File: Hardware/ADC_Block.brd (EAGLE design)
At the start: 30.5 x 44.5 mm, 34 parts, among them U1 ADS1015, U2 PCA9306, U3 3.3V

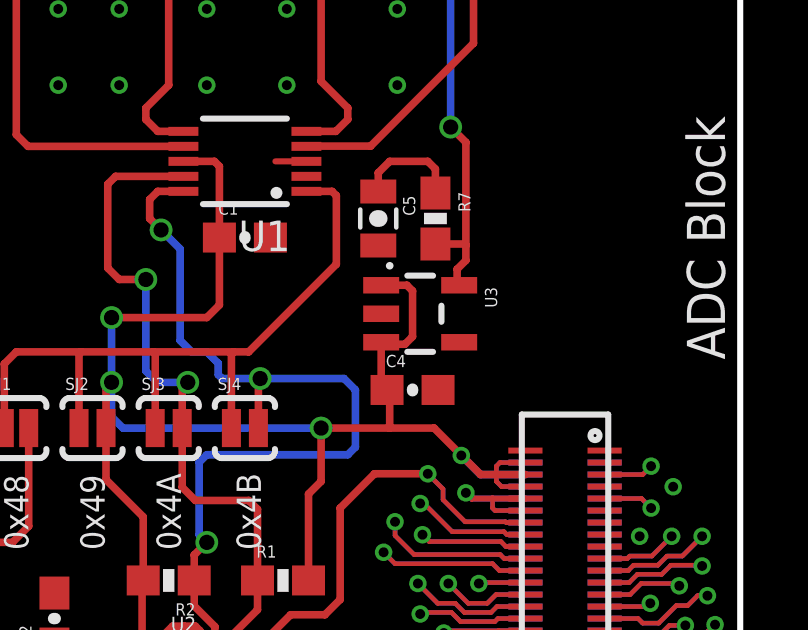
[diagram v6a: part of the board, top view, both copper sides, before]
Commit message: Moved pin 1 markers to outside packages on IC and Hirose connectors.
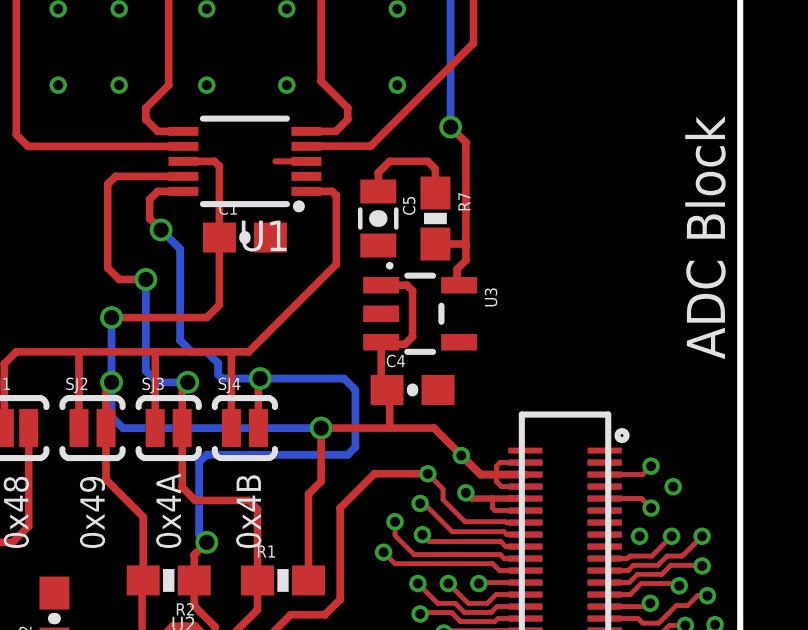
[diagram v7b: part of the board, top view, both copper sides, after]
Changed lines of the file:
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@@
 <layer number="45" name="Holes" color="7" fill="1" visible="yes" active="yes"/>
 <layer number="46" name="Milling" color="3" fill="1" visible="no" active="yes"/>
-<layer number="47" name="Measures" color="7" fill="1" visible="no" active="yes"/>
+<layer number="47" name="Measures" color="7" fill="1" visible="yes" active="yes"/>
 <layer number="51" name="tDocu" color="6" fill="1" visible="yes" active="yes"/>
 <layer number="52" name="bDocu" color="7" fill="1" visible="no" active="yes"/>
@@
 </class>
 </classes>
-<designrules name="Gold_Phoenix_Standard_Spec_2_layer">
-<description language="en">&lt;b&gt;EAGLE Design Rules&lt;/b&gt;
+<designrules name="SparkFun-2-layer-FAB-LIMIT">
+<description language="en">&lt;b&gt;SparkFun 2 Layer Design Rule Checks - STANDARD/TIGHT/FAB-LIMIT&lt;/b&gt;
 &lt;p&gt;
-The default Design Rules have been set to cover
-a wide range of applications. Your particular design
-may have different requirements, so please make the
-necessary adjustments and save your customized
-design rules under a new name.</description>
+These rules have been curated by SparkFuns DFM commitee. After doing much research, communicating with our multiple fab houses, and getting quotes of various designs, we have compiled three DRU files.
+&lt;p&gt;
+&lt;b&gt;STANDARD:&lt;/b&gt; This is more of a &quot;best case scenario&quot; set of limitations. If your design has the space, and/or you have the time to work within these parameters, please do. Larger trace width and clearance makes for easier visual inspection of the PCB while troubleshooting (useful in production and to the end user). It also allows for better ability to hack a trace (if you are crazy enough to scrape away the mask and solder to a trace). Another thing to keep in mind is that more metal is just more robust.
+&lt;p&gt;
+&lt;b&gt;TIGHT:&lt;/b&gt; This is where cost comes into play. We have found that most fab houses begin to add extra charges when you go smaller than these specs. In some cases, going to less than 15 mil trace can increase the cost by 10%. (This is why we have set the min drill on this DRU to 15 mil) Same story for traces thinner than 7 mil. To avoid those extra charges, then stay within the rules of this DRU.
+&lt;p&gt;
+&lt;b&gt;FAB-LIMIT:&lt;/b&gt; These set of rules are at the very limit of most fab houses capabilities. You will pay more for these specs, and it should be used on designs that have a darned good reason to need 4 mil vias and 4 mil traces.
+&lt;p&gt;
+**NOTE Clearance, Distance, Sizes, and Restring are all set to different limits in each of these three DRU files. Please compare the files within the CAM job editor window of eagle to see all the numbers.
+&lt;p&gt;
+***NOTE, Please set your Net Classes to default (0mil for all settings), so that it won't effect the DRC when you run it with these settings.</description>
 <param name="layerSetup" value="(1*16)"/>
 <param name="mtCopper" value="0.035mm 0.035mm 0.035mm 0.035mm 0.035mm 0.035mm 0.035mm 0.035mm 0.035mm 0.035mm 0.035mm 0.035mm 0.035mm 0.035mm 0.035mm 0.035mm"/>
 <param name="mtIsolate" value="1.5mm 0.15mm 0.2mm 0.15mm 0.2mm 0.15mm 0.2mm 0.15mm 0.2mm 0.15mm 0.2mm 0.15mm 0.2mm 0.15mm 0.2mm"/>
-<param name="mdWireWire" value="5mil"/>
-<param name="mdWirePad" value="5mil"/>
-<param name="mdWireVia" value="5mil"/>
-<param name="mdPadPad" value="5mil"/>
-<param name="mdPadVia" value="5mil"/>
-<param name="mdViaVia" value="5mil"/>
-<param name="mdSmdPad" value="5mil"/>
-<param name="mdSmdVia" value="5mil"/>
-<param name="mdSmdSmd" value="5mil"/>
+<param name="mdWireWire" value="4mil"/>
+<param name="mdWirePad" value="4mil"/>
+<param name="mdWireVia" value="4mil"/>
+<param name="mdPadPad" value="4mil"/>
+<param name="mdPadVia" value="4mil"/>
+<param name="mdViaVia" value="4mil"/>
+<param name="mdSmdPad" value="4mil"/>
+<param name="mdSmdVia" value="4mil"/>
+<param name="mdSmdSmd" value="4mil"/>
 <param name="mdViaViaSameLayer" value="8mil"/>
 <param name="mnLayersViaInSmd" value="2"/>
-<param name="mdCopperDimension" value="8mil"/>
-<param name="mdDrill" value="8mil"/>
+<param name="mdCopperDimension" value="4mil"/>
+<param name="mdDrill" value="4mil"/>
 <param name="mdSmdStop" value="0mil"/>
-<param name="msWidth" value="5mil"/>
+<param name="msWidth" value="4mil"/>
 <param name="msDrill" value="6mil"/>
 <param name="msMicroVia" value="9.99mm"/>
@@
 <param name="rlMinPadTop" value="5mil"/>
 <param name="rlMaxPadTop" value="20mil"/>
-<param name="rlMinPadInner" value="10mil"/>
+<param name="rlMinPadInner" value="6mil"/>
 <param name="rlMaxPadInner" value="20mil"/>
 <param name="rlMinPadBottom" value="5mil"/>
@@
 <param name="rlMinViaOuter" value="5mil"/>
 <param name="rlMaxViaOuter" value="20mil"/>
-<param name="rlMinViaInner" value="10mil"/>
+<param name="rlMinViaInner" value="6mil"/>
 <param name="rlMaxViaInner" value="20mil"/>
 <param name="rlMinMicroViaOuter" value="4mil"/>
@@
 <via x="9.144" y="13.716" extent="1-16" drill="0.508"/>
 <wire x1="16.02" y1="33.02" x2="14.986" y2="33.02" width="0.2032" layer="1"/>
+<wire x1="25.96" y1="21.3798" x2="25.96" y2="21.38" width="0" layer="19" extent="1-16"/>
+<wire x1="25.96" y1="20.98" x2="25.96" y2="21.38" width="0" layer="19" extent="16-16"/>
+<wire x1="25.96" y1="20.9798" x2="25.96" y2="20.98" width="0" layer="19" extent="1-16"/>
+<wire x1="25.96" y1="20.58" x2="25.96" y2="20.98" width="0" layer="19" extent="16-16"/>
+<wire x1="25.96" y1="20.5798" x2="25.96" y2="20.58" width="0" layer="19" extent="1-16"/>
+<wire x1="25.96" y1="20.18" x2="25.96" y2="20.58" width="0" layer="19" extent="16-16"/>
+<wire x1="25.96" y1="20.1798" x2="25.96" y2="20.18" width="0" layer="19" extent="1-16"/>
+<wire x1="25.96" y1="22.1798" x2="25.96" y2="21.38" width="0" layer="19" extent="1-16"/>
 </signal>
 <signal name="VSYS">

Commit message: Changed solder jumper to make I2C_6 default
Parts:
- SJ5, SJ6: device SparkFun-Passives:PAD-JUMPER-3-2OF3_NC_BY_PASTE_YES_SILK_FULL_BOX -> SparkFun-Passives:PAD-HUMPER-3-1&2_NC_BY_PASTE_YES_SILK_FULL_BOX
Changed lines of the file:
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@@
 <?xml version="1.0" encoding="utf-8"?>
 <!DOCTYPE eagle SYSTEM "eagle.dtd">
-<eagle version="7.2.0">
+<eagle version="7.3.0">
 <drawing>
 <settings>
@@
 <layer number="45" name="Holes" color="7" fill="1" visible="yes" active="yes"/>
 <layer number="46" name="Milling" color="3" fill="1" visible="no" active="yes"/>
-<layer number="47" name="Measures" color="7" fill="1" visible="yes" active="yes"/>
+<layer number="47" name="Measures" color="7" fill="1" visible="no" active="yes"/>
 <layer number="51" name="tDocu" color="6" fill="1" visible="yes" active="yes"/>
 <layer number="52" name="bDocu" color="7" fill="1" visible="no" active="yes"/>
@@
 <attribute name="PROD_ID" value="CAP-11330" x="18.415" y="31.115" size="1.778" layer="27" rot="R270" display="off"/>
 </element>
-<element name="SJ5" library="SparkFun-Passives" package="PAD-JUMPER-3-2OF3_NC_BY_PASTE_YES_SILK_FULL_BOX" value="SDA_SEL" x="16.637" y="8.763" rot="R180"/>
-<element name="SJ6" library="SparkFun-Passives" package="PAD-JUMPER-3-2OF3_NC_BY_PASTE_YES_SILK_FULL_BOX" value="SCL_SEL" x="16.637" y="10.922" rot="R180"/>
+<element name="SJ5" library="SparkFun-Passives" package="PAD-HUMPER-3-1&amp;2_NC_BY_PASTE_YES_SILK_FULL_BOX" value="SDA_SEL" x="16.637" y="8.763" rot="R180"/>
+<element name="SJ6" library="SparkFun-Passives" package="PAD-HUMPER-3-1&amp;2_NC_BY_PASTE_YES_SILK_FULL_BOX" value="SCL_SEL" x="16.637" y="10.922" rot="R180"/>
 <element name="R7" library="SparkFun-Resistors" package="0603-RES" value="0.27" x="20.32" y="31.115" rot="R270">
 <attribute name="PROD_ID" value="RES-08787" x="20.32" y="31.115" size="1.778" layer="27" font="vector" ratio="15" rot="R270" display="off"/>
